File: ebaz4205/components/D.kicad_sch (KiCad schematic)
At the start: 1 part

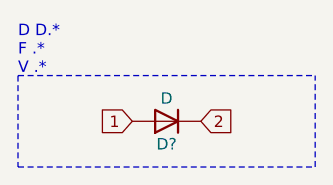
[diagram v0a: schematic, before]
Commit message: Provided all component symbols.
Symbol libraries are available as subdirectories in ebaz4205/components/

U23 is still unknown, so a placeholder symbol was provided.
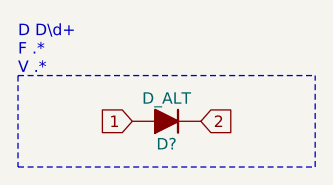
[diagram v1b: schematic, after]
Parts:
- removed D?: D, symbol Device:D
- added D?: D_ALT, symbol Device:D_ALT
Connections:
- net 1: now also D?.2 (A)
- net 2: now also D?.1 (K)
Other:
- note added: "D D\d+ F .* V .*"
- note removed: "D D.* F .* V .*"
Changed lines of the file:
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@@
     (stroke (width 0) (type dash) (color 0 0 0 0))
   )
-  (text "D D.*\nF .*\nV .*" (at 0 0 0)
+  (text "D D\\d+\nF .*\nV .*" (at 0 0 0)
     (effects (font (size 1.27 1.27)) (justify left bottom))
   )
@@
     (effects (font (size 1.27 1.27)) (justify left))
   )
-  (symbol (lib_id "Device:D") (at 16.51 5.08 180) (unit 1)
+  (symbol (lib_id "Device:D_ALT") (at 16.51 5.08 180) (unit 1)
     (in_bom yes) (on_board yes)
     (property "Reference" "D?" (id 0) (at 16.51 7.62 0))
-    (property "Value" "D" (id 1) (at 16.51 2.54 0))
+    (property "Value" "D_ALT" (id 1) (at 16.51 2.54 0))
     (property "Footprint" "" (id 2) (at 16.51 5.08 0)
       (effects (font (size 1.27 1.27)) hide)
@@
   )
   (symbol_instances
-    (path "/5e08f97d-fa45-4e39-a308-17279ec73809"
-      (reference "D?") (unit 1) (value "D") (footprint "")
+    (path "/4b23dc1d-1cee-4e18-91f9-392beea5e7b2"
+      (reference "D?") (unit 1) (value "D_ALT") (footprint "")
     )
   )
